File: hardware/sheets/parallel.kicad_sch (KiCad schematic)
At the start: 22 parts, among them J1 DB25_Pins, U1 74LVC574A, U10 74HC32, U12 74HC00, U2 74LVC574A, U3 74LVC244A, U4 74LVC245A, U5 74LVC244A, U6 74HC138, U9 74AHC14

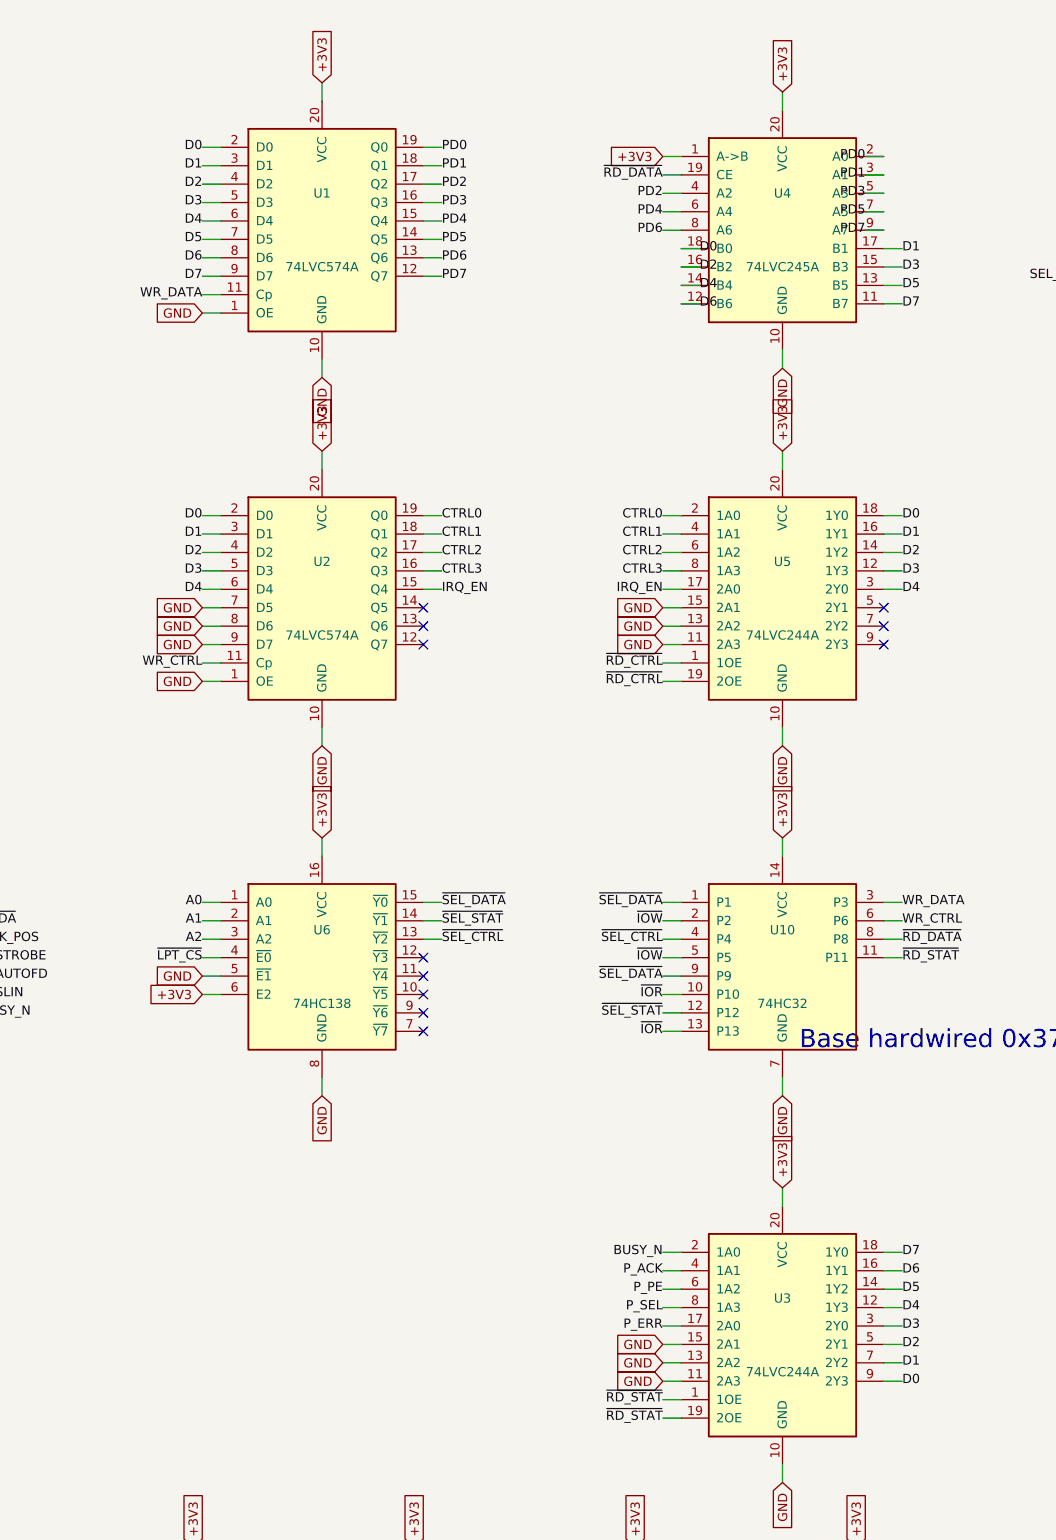
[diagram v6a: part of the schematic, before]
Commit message: KiCad 10 symbol support: read sharded .kicad_symdir libraries
The KiCad snap (which supplied the KiCad 9 monolithic .kicad_sym libs)
is gone; the KiCad 10 AppImage ships its libraries in the new sharded
format instead: <Lib>.kicad_symdir/ directories of one-symbol files.

- mxsch: lib_source() resolves a .kicad_sym path to the file or its
  .kicad_symdir sibling; SymbolLib.load() loads every file in a symdir
  (extends resolution runs after all files, since base and derived
  symbols live in separate files); kicad_symdir() falls back to
  ~/.local/share/kicad/<ver>/symbols (populated once from the AppImage)
- build/pins/gensym: route existence checks + copy_symbol through it
- power/supervisor: USB-C/USB-A shield pin renamed S1/5 -> SH in the
  KiCad 10 libs (the one real symbol-content change; still GND)
- selftest: netlist checker now tolerates KiCad 10's multiline netlist
  format (it silently found nothing since the CLI moved to 10)
- regenerate all sheets + mini-xt.kicad_sym from KiCad 10 sources: the
  churn is embedded-symbol format tokens only. Verified: ERC 0/0,
  before/after netlists have identical net->node sets (736 nets, only
  the shield-pin rename), double-build stays byte-identical, all seven
  custom symbols pin-identical after gensym regen.

Co-Authored-By: Claude Fable 5 <noreply@anthropic.com>
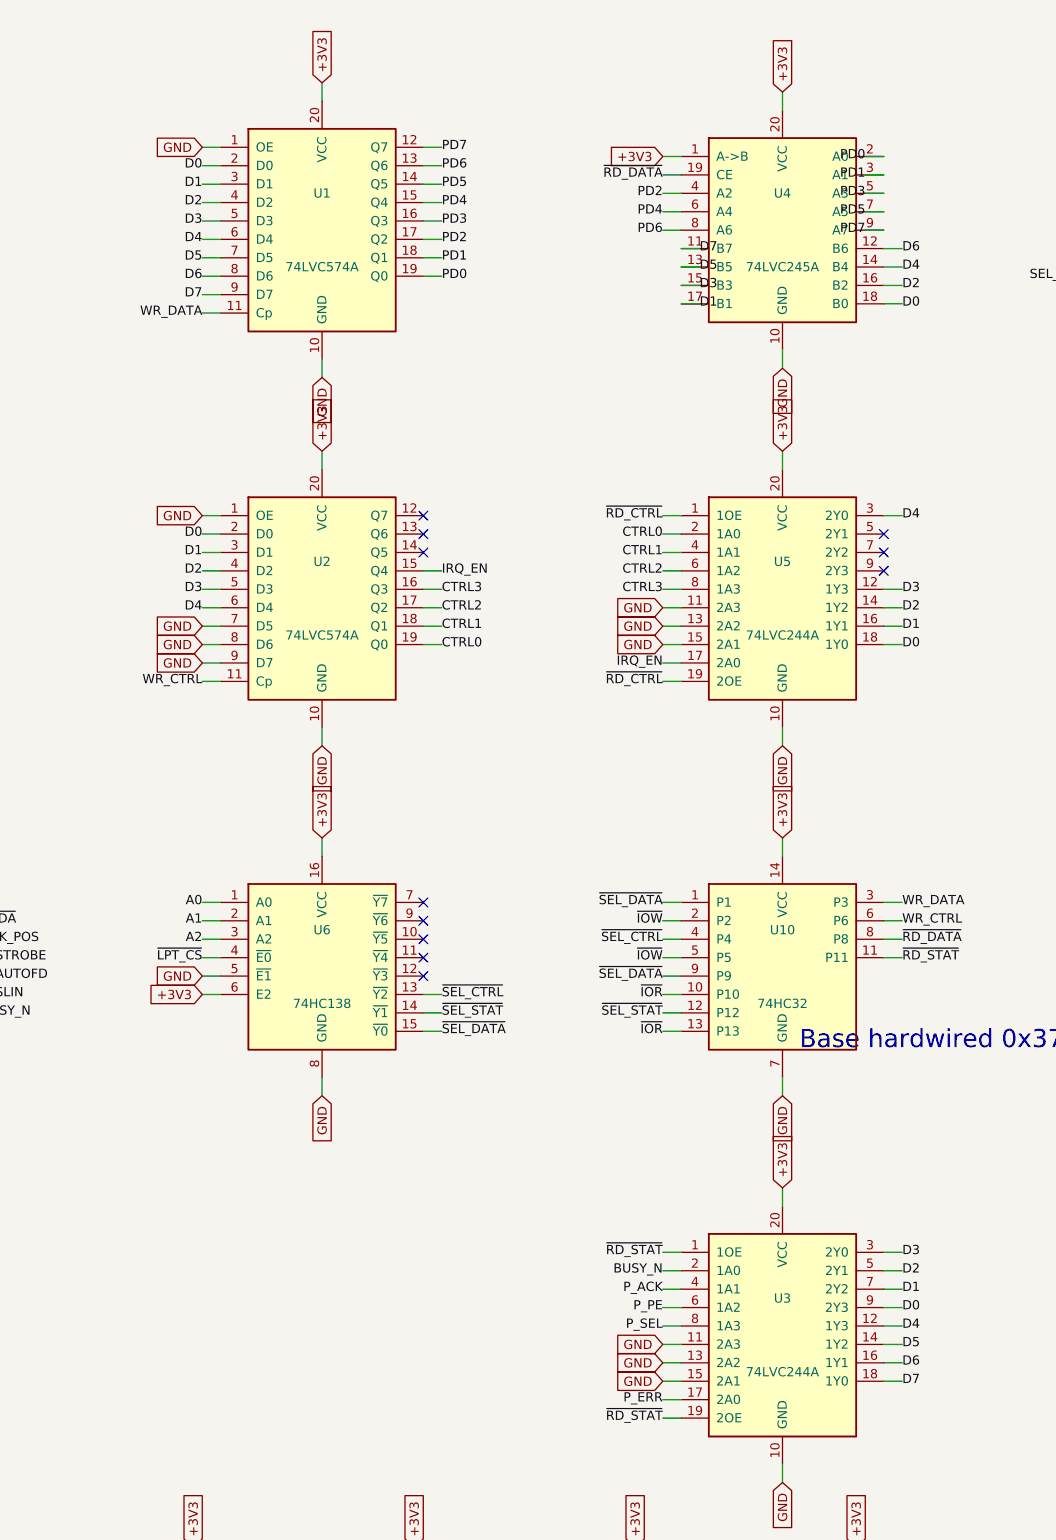
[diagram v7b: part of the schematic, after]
